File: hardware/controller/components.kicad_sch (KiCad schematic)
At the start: 11 parts, among them U5 AP2112K-3.3, U6 SN74LVC1T45DBV

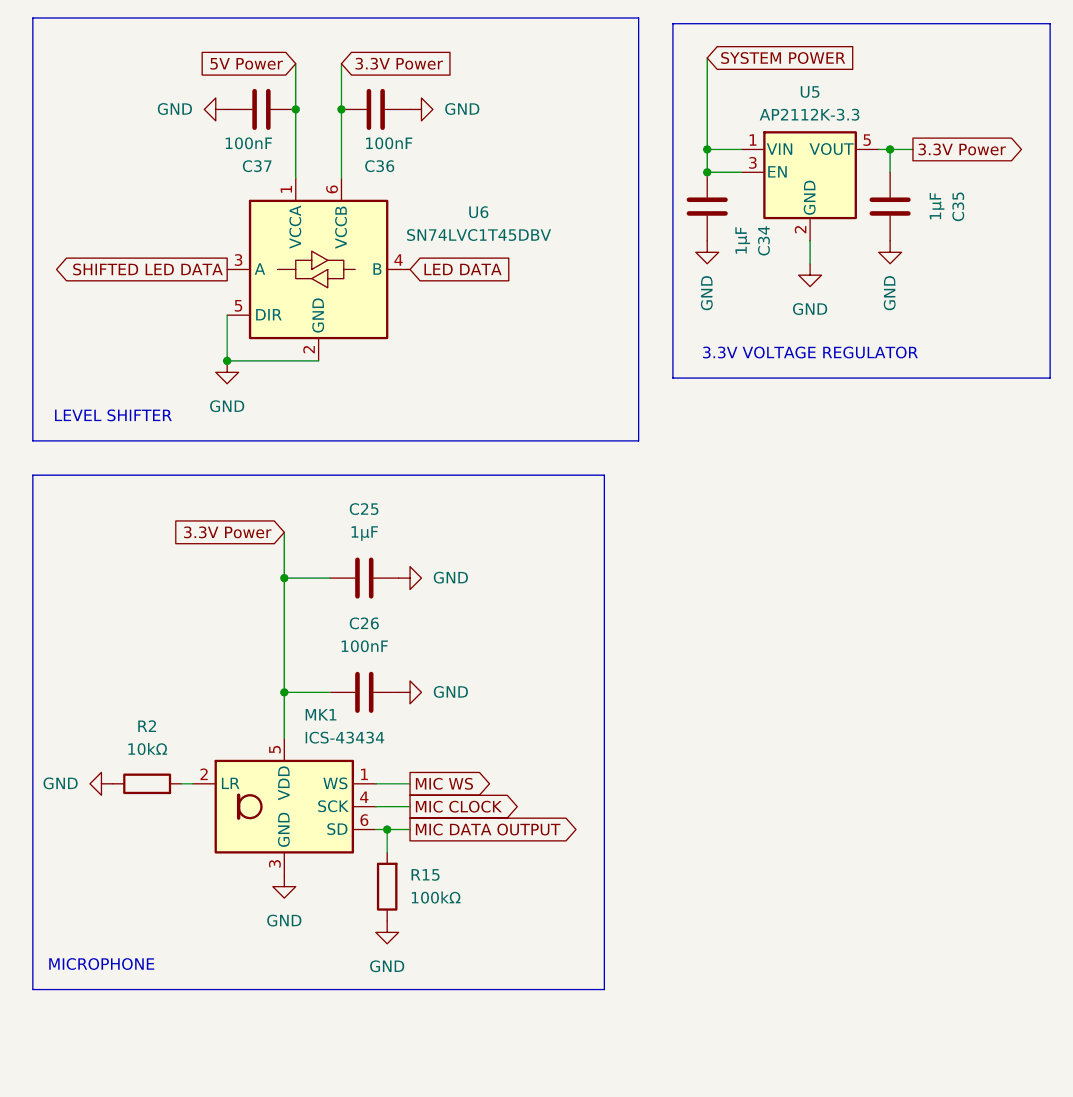
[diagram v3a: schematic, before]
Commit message: placing more components for controller board
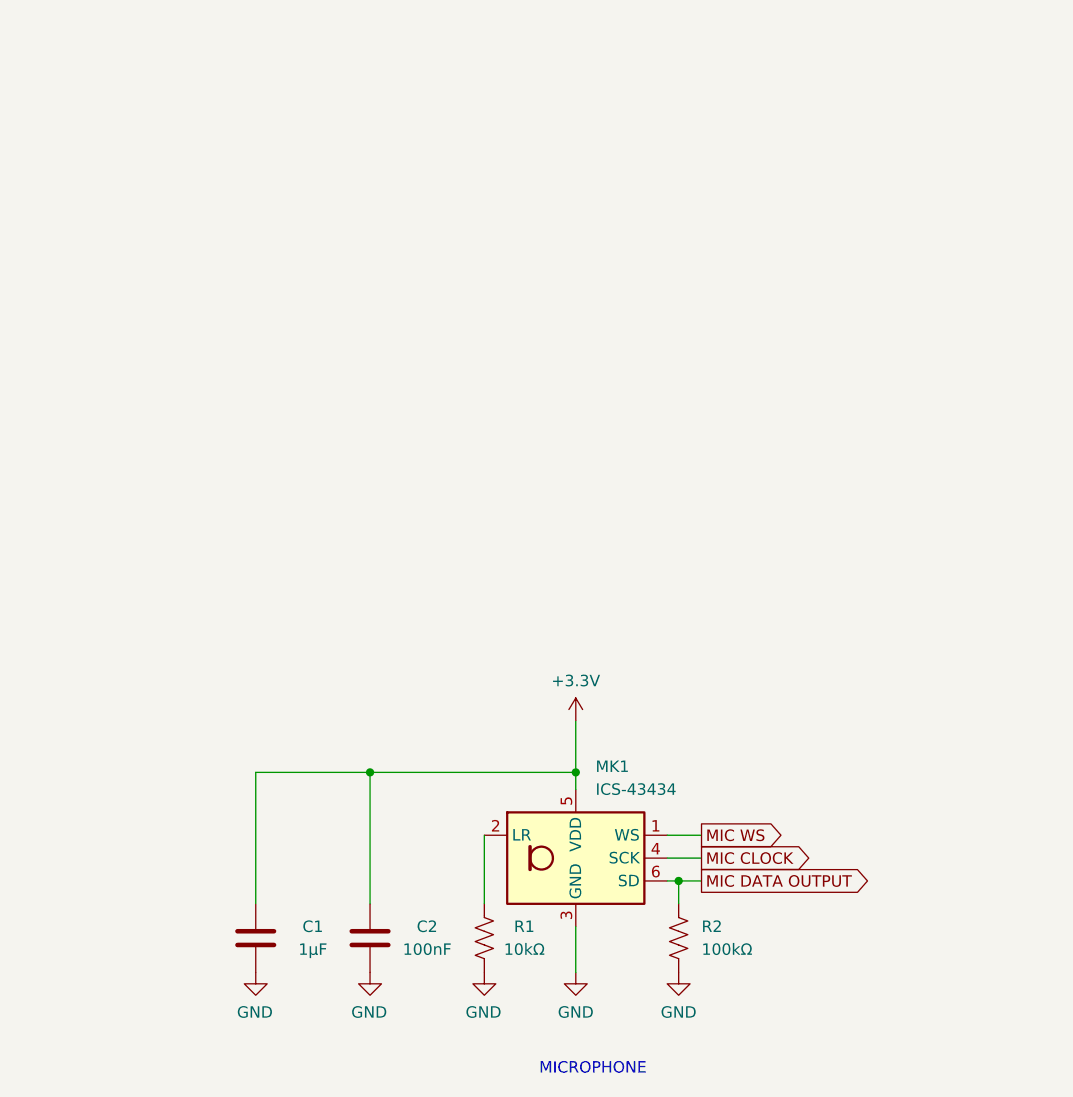
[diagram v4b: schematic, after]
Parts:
- removed C25, C34, C35: 1µF, Capacitor_SMD:C_0603_1608Metric, symbol Device:C
- removed C26, C36, C37: 100nF, Capacitor_SMD:C_0402_1005Metric, symbol Device:C
- removed U5: AP2112K-3.3, Package_TO_SOT_SMD:SOT-23-5, symbol Regulator_Linear:AP2112K-3.3
- removed U6: SN74LVC1T45DBV, Package_TO_SOT_SMD:SOT-23-6, symbol Logic_LevelTranslator:SN74LVC1T45DBV
- added C1: 1µF, Capacitor_SMD:C_0603_1608Metric, symbol Device:C
- added C2: 100nF, Capacitor_SMD:C_0402_1005Metric, symbol Device:C
- R1: renamed from R2; symbol Device:R -> Device:R_US
- R2: renamed from R15; symbol Device:R -> Device:R_US
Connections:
- net GND: now also C1.2, C2.2
- net 3.3V Power renamed +3.3V
- net +3.3V: now also C1.1, C2.1
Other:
- note removed: "3.3V VOLTAGE REGULATOR"
- note removed: "LEVEL SHIFTER"
- moved on the sheet: MK1

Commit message: more controller board work, consolidation/revision of design
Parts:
- removed C1: 1µF, Capacitor_SMD:C_0603_1608Metric, symbol Device:C
- removed C2: 100nF, Capacitor_SMD:C_0402_1005Metric, symbol Device:C
- removed MK1: ICS-43434, Sensor_Audio:InvenSense_ICS-43434-6_3.5x2.65mm, symbol Sensor_Audio:ICS-43434
- removed R1: 10kΩ, Resistor_SMD:R_0603_1608Metric, symbol Device:R_US
- removed R2: 100kΩ, Resistor_SMD:R_0603_1608Metric, symbol Device:R_US
- added U7: baochip1x, baochip:WLCSP-71_9x8_4.062x3.762mm, symbol baochip:baochip1x
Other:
- note removed: "MICROPHONE"

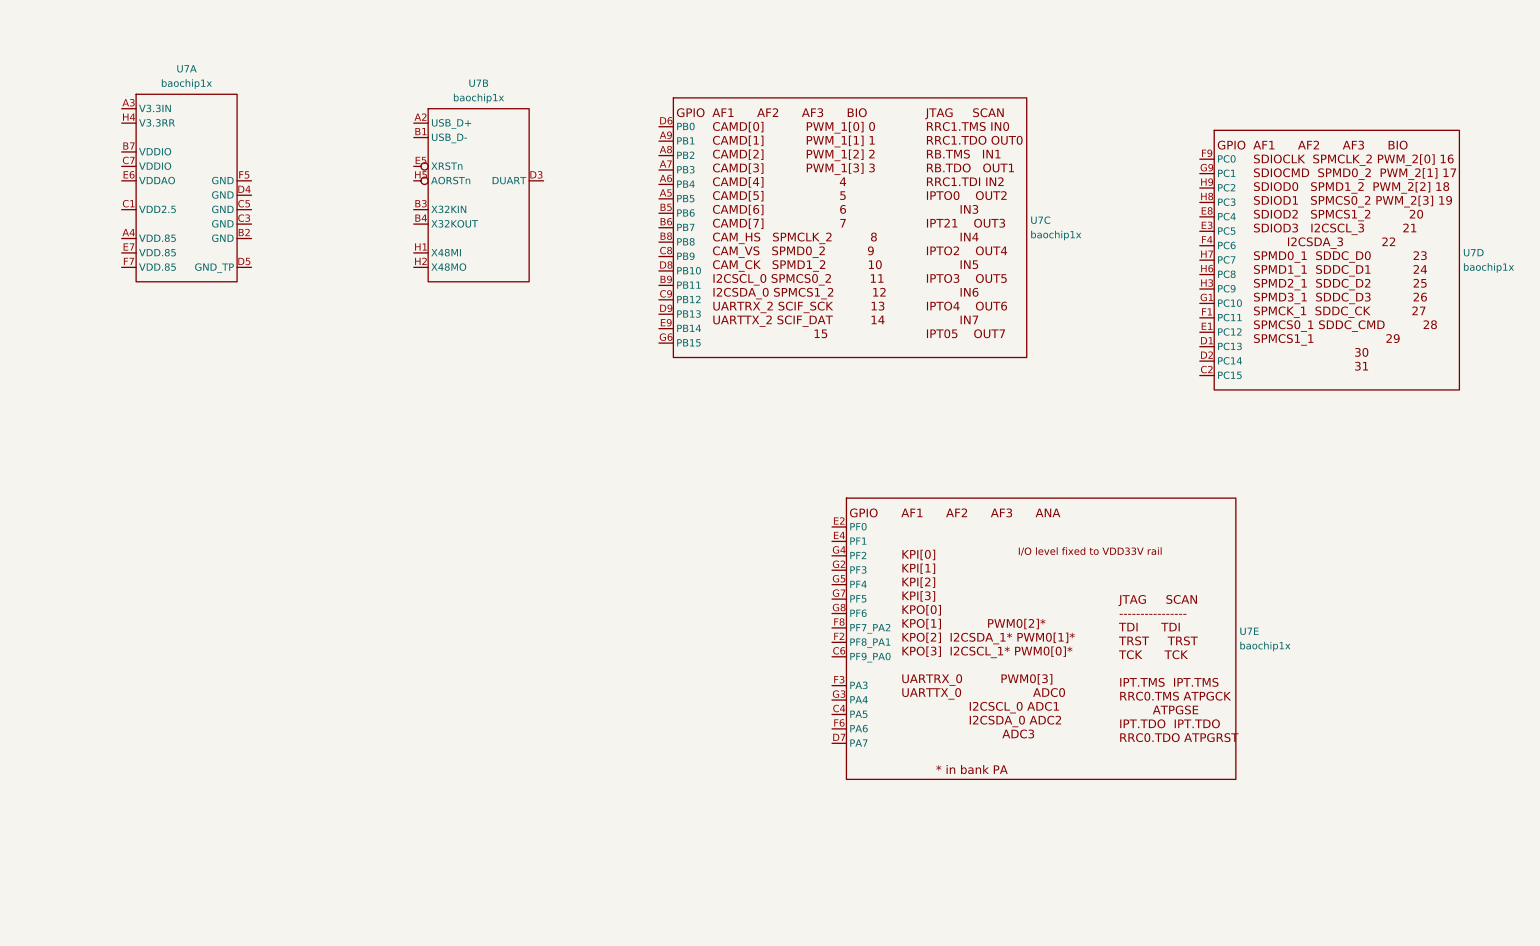
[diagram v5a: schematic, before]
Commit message: schematic renaming
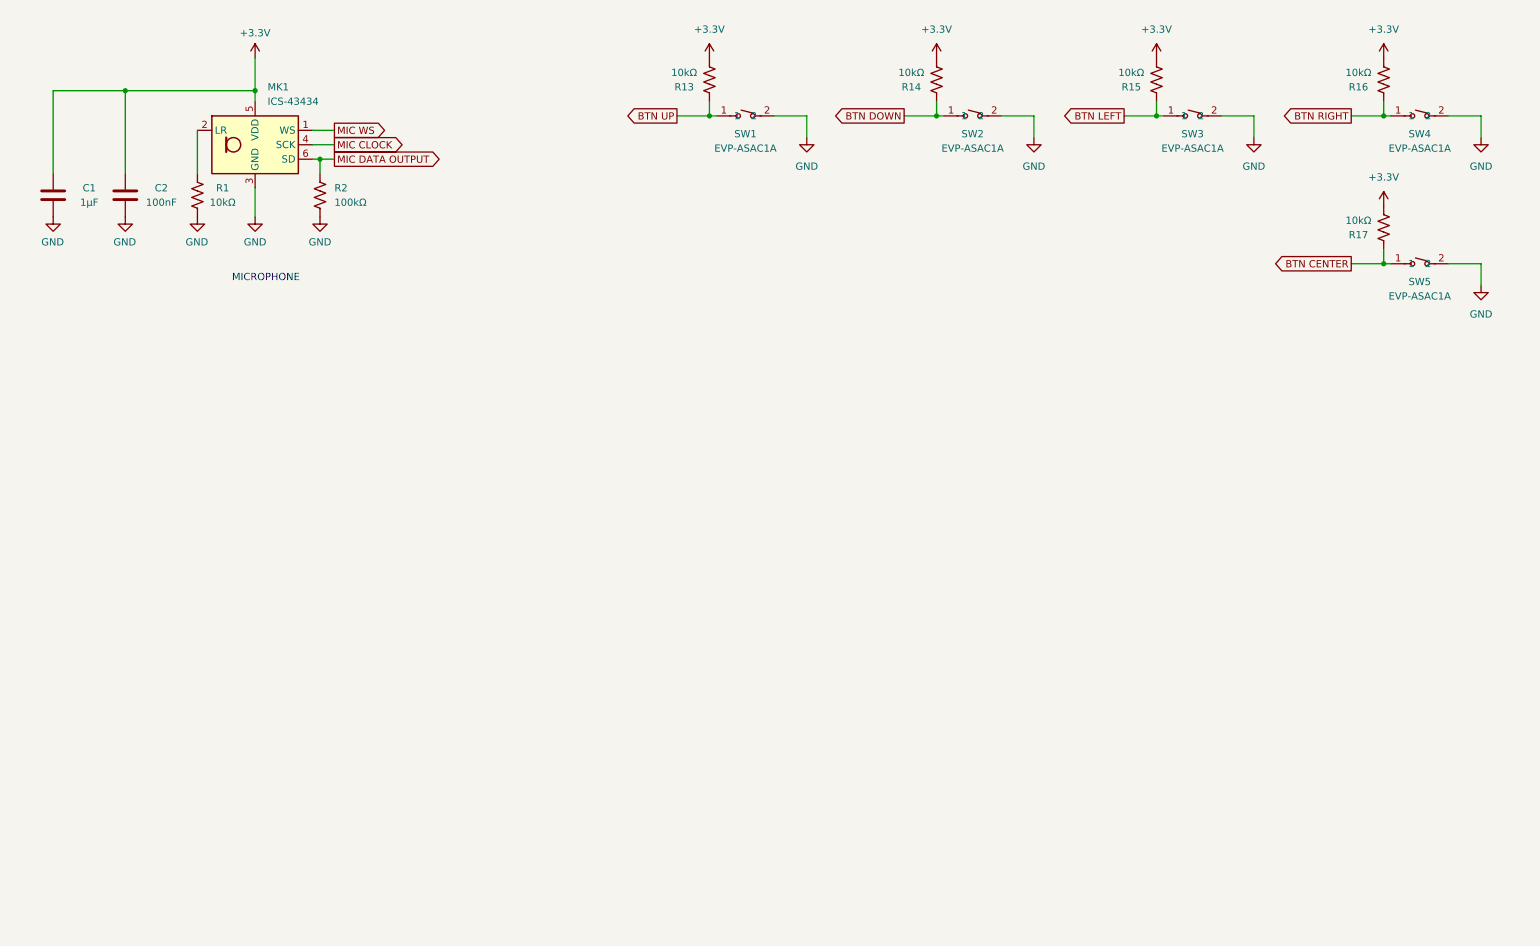
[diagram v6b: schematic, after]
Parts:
- removed U7: baochip1x, baochip:WLCSP-71_9x8_4.062x3.762mm, symbol baochip:baochip1x
- added C1: 1µF, Capacitor_SMD:C_0603_1608Metric, symbol Device:C
- added C2: 100nF, Capacitor_SMD:C_0402_1005Metric, symbol Device:C
- added MK1: ICS-43434, Sensor_Audio:InvenSense_ICS-43434-6_3.5x2.65mm, symbol Sensor_Audio:ICS-43434
- added R1, R13, R14, R15, R16, R17: 10kΩ, Resistor_SMD:R_0603_1608Metric, symbol Device:R_US
- added R2: 100kΩ, Resistor_SMD:R_0603_1608Metric, symbol Device:R_US
- added SW1, SW2, SW3, SW4, SW5: EVP-ASAC1A, easyeda2kicad:SW-SMD_PANASONIC_EVPASXXX, symbol easyeda2kicad:EVP-ASAC1A
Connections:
- new net: MK1.2 (LR), R1.2
- new net +3.3V: C1.1, C2.1, MK1.5 (VDD), R13.1, R14.1, R15.1, R16.1, R17.1
- new net BTN CENTER: R17.2, SW5.1
- new net BTN DOWN: R14.2, SW2.1
- new net BTN LEFT: R15.2, SW3.1
- new net BTN RIGHT: R16.2, SW4.1
- new net BTN UP: R13.2, SW1.1
- new net GND: C1.2, C2.2, MK1.3 (GND), R1.1, R2.1, SW1.2, SW2.2, SW3.2, SW4.2, SW5.2
- new net MIC CLOCK: MK1.4 (SCK)
- new net MIC DATA OUTPUT: MK1.6 (SD), R2.2
- new net MIC WS: MK1.1 (WS)
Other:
- note added: "MICROPHONE"

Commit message: more controller board work
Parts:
- added C15: 100nF, Capacitor_SMD:C_0402_1005Metric, symbol Device:C
- added C16: 1µF, Capacitor_SMD:C_0603_1608Metric, symbol Device:C
- added CGQ1: IRM-H638T/TR2, easyeda2kicad:SENSOR-SMD_IRM-H638T-TR2-TL, symbol easyeda2kicad:IRM-H638T_TR2
- added R18, R19: 10kΩ, Resistor_SMD:R_0603_1608Metric, symbol Device:R_US
- added R20: 100Ω, Resistor_SMD:R_0603_1608Metric, symbol Device:R_US
- added SW6: CL-SB-13A-02T, easyeda2kicad:SW-SMD_CL-SB-13A-0X, symbol easyeda2kicad:CL-SB-13A-02T
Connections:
- net +3.3V: now also R18.1, R19.1, R20.2, SW6.1, SW6.4
- net GND: now also C15.2, C16.2, CGQ1.1 (GND), CGQ1.2 (GND), R18.2, R19.2, SW6.2, SW6.3
- new net: C15.1, C16.1, CGQ1.4 (VCC), R20.1
- new net IR SENSOR DATA: CGQ1.3 (VOUT)

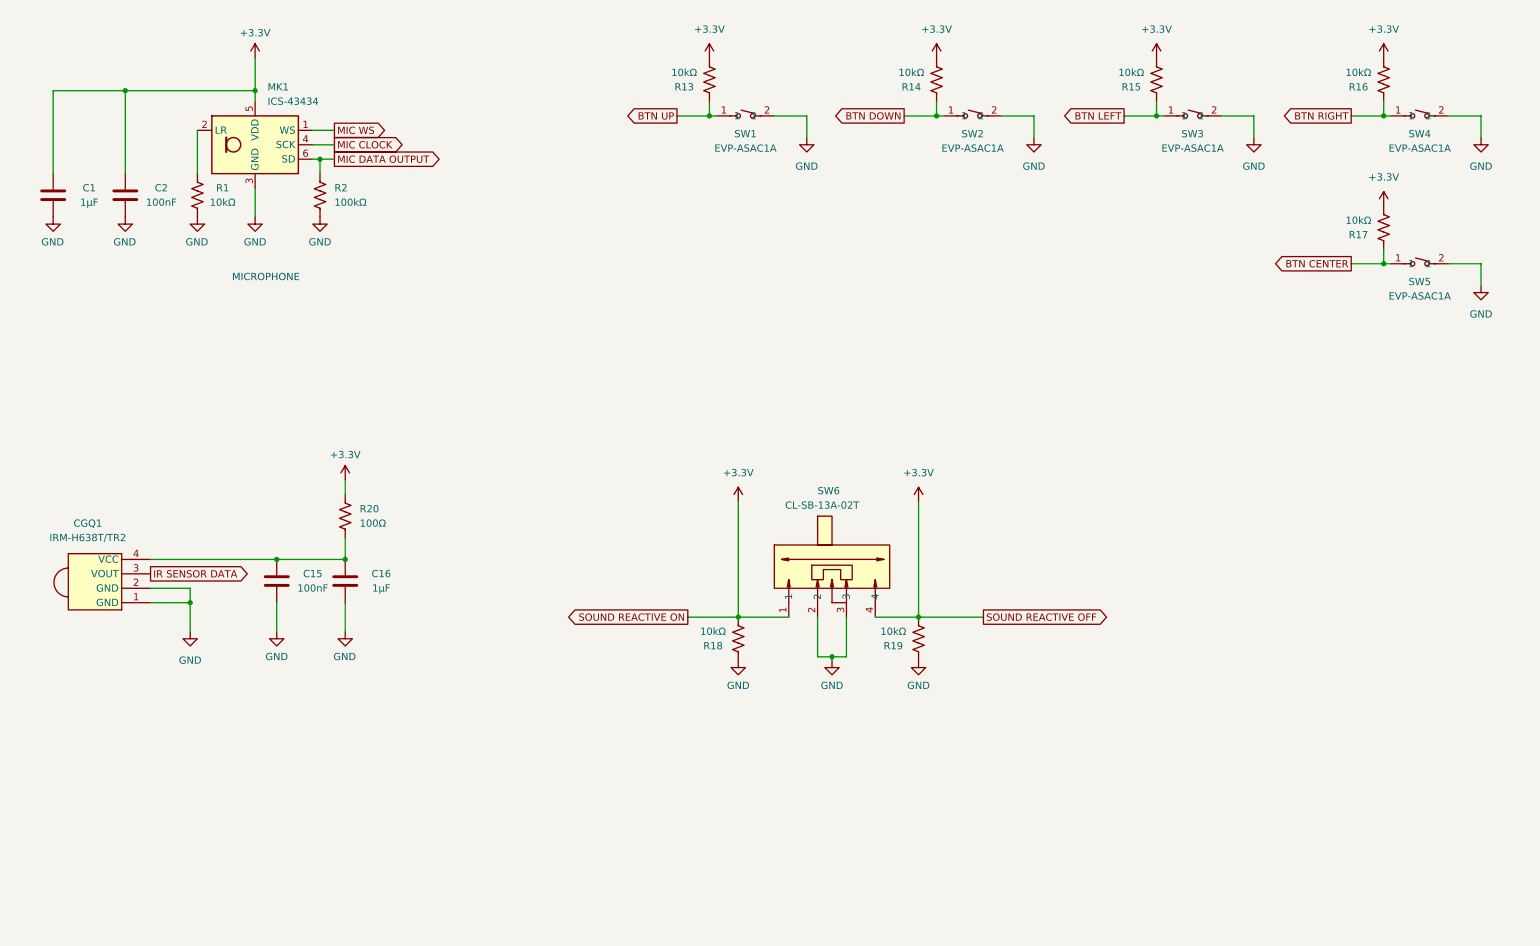
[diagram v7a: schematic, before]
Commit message: re-order the numbers on the schematic for tidiness
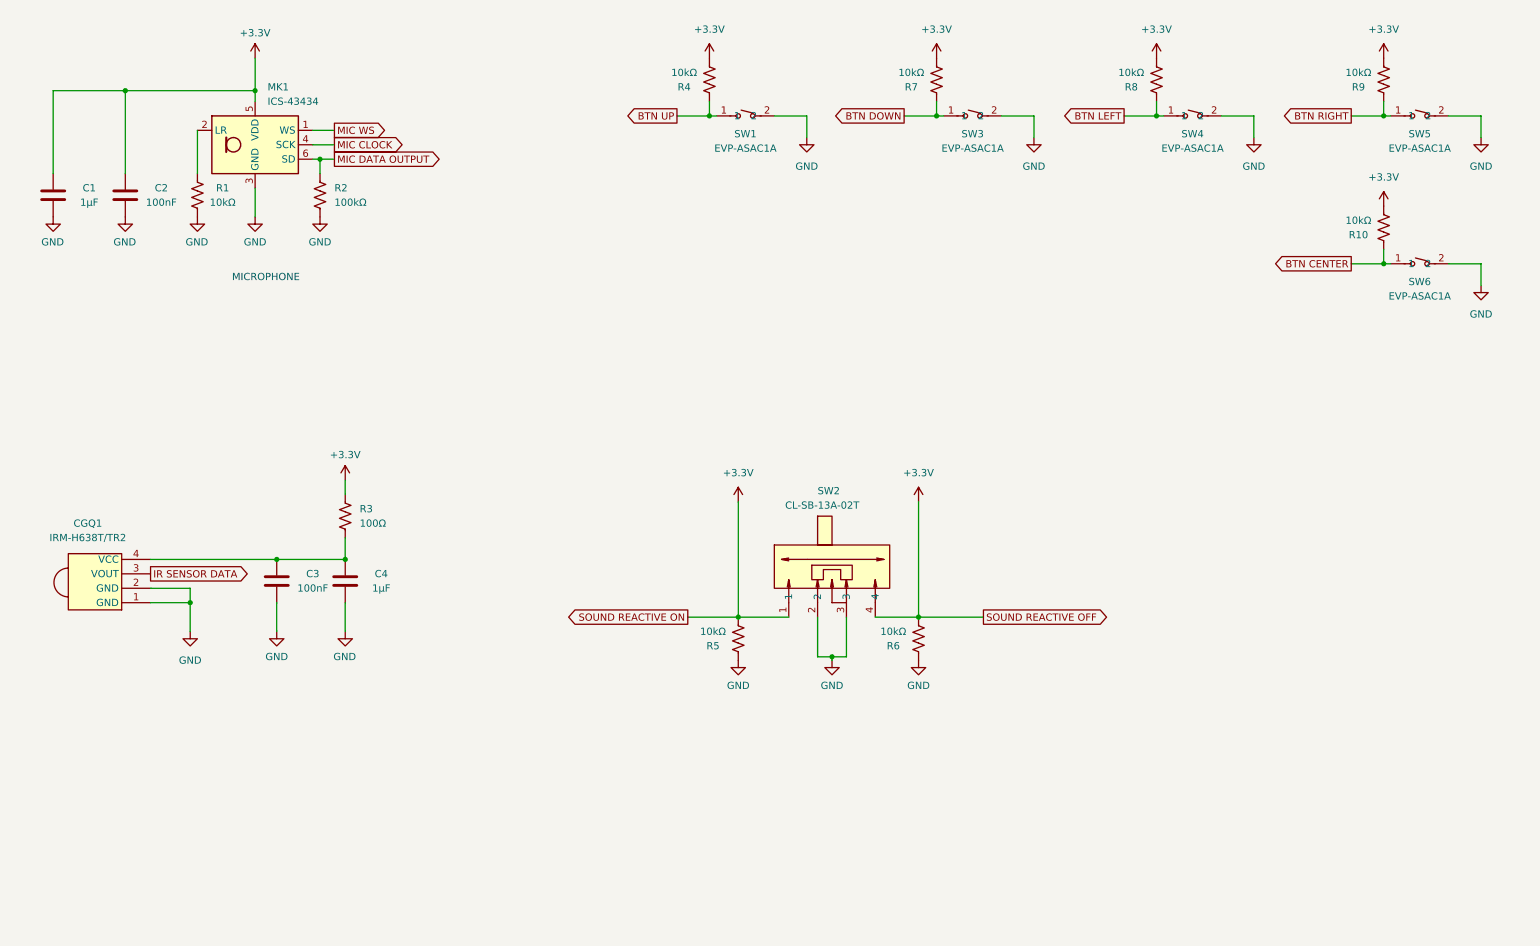
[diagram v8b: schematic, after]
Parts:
- renumbered C15 to C3, C16 to C4, R17 to R10, R20 to R3, R13 to R4, R18 to R5, R19 to R6, R14 to R7, R15 to R8, R16 to R9, SW6 to SW2, SW2 to SW3, SW3 to SW4, SW4 to SW5, SW5 to SW6
